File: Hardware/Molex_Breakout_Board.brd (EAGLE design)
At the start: 31.8 x 36.8 mm, 14 parts

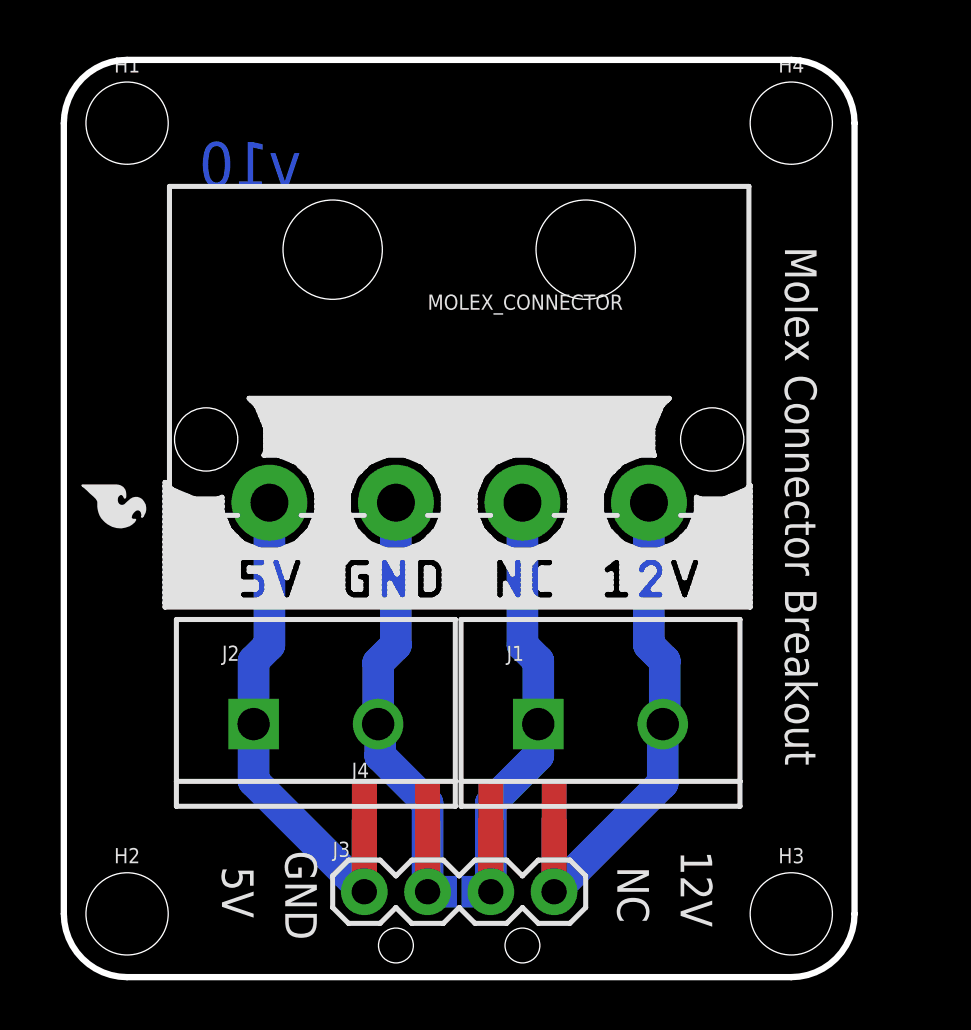
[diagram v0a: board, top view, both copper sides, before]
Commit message: Update Board File
-update text to standard buzzard
-remove negasilk and replace with dashed outline of straight molex connector
-add top thick trace on top
-adjust package so that NC is GND
-remove jumper on bottom of board
-adjust size so mounting holes are not in the way of right angle connector
-adjust measurements based on new size
-adjust text so that it is not overlapping on the mounting holes
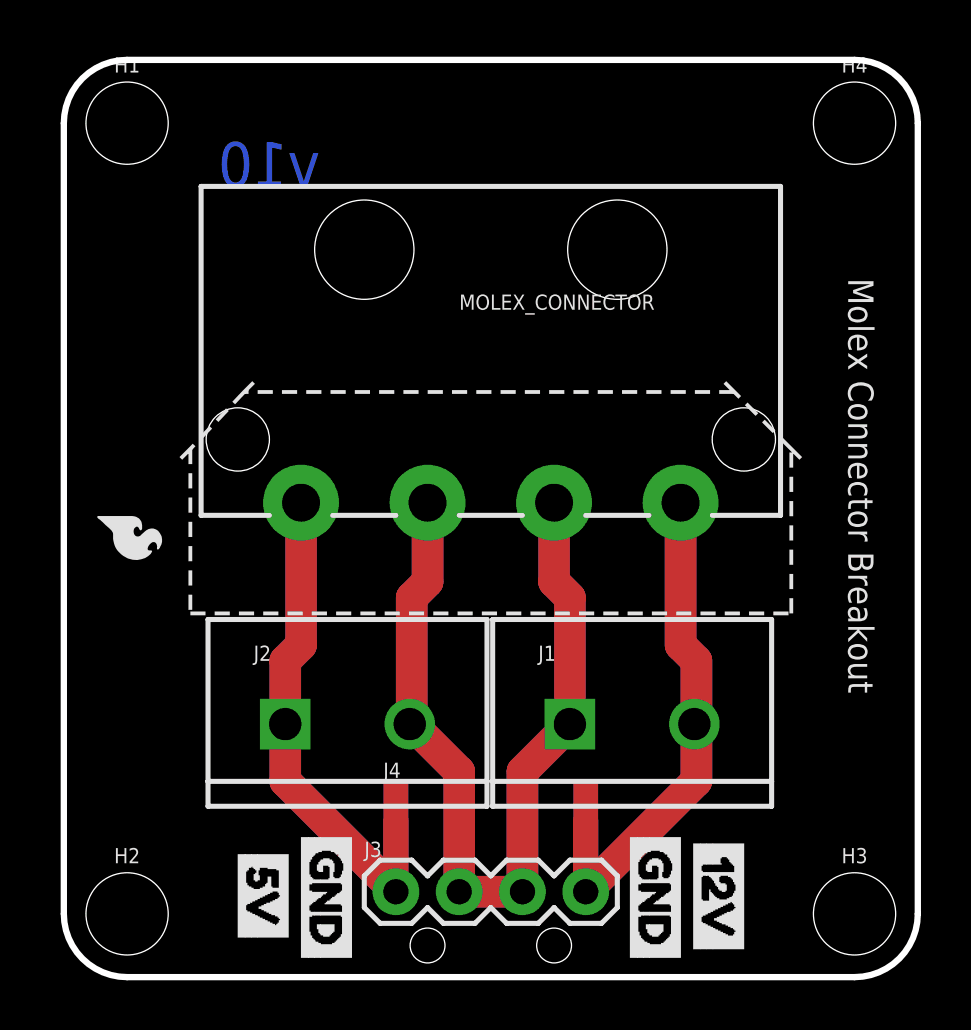
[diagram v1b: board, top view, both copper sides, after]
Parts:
- removed JP1: JUMPER-SMT_2_NO_NO-SILK, SparkFun-Jumpers:SMT-JUMPER_2_NO_NO-SILK
- moved H3 2.54 mm to (31.8, 2.54)
- moved H4 2.54 mm to (31.8, 34.3)
- moved LOGO3 1.42 mm to (1.02, 18.8)
- moved J3 1.27 mm to (13.3, 3.43)
- moved J2 1.27 mm to (8.89, 10.2)
- moved J1 1.27 mm to (20.3, 10.2)
- moved J4 1.27 mm to (17.1, 1.27)
- moved LOGO1 1.27 mm to (17.1, 27.9)
- moved LOGO2 1.27 mm to (23.5, 20.3)
- moved MOLEX_CONNECTOR 1.27 mm to (17.1, 21.6)
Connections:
- removed net NC: J1.1, J3.3, J4.3, JP1.2, MOLEX_CONNECTOR.NC
- net GND: now also J1.1, J3.3, J4.3, MOLEX_CONNECTOR.GND@1, MOLEX_CONNECTOR.GND@2; no longer JP1.1, MOLEX_CONNECTOR.GND
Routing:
- net GND: track 20.4 -> 77.8 mm
- net NC: track 20.4 -> 0.00 mm
- net 12V: track 20.6 -> 38.5 mm
- net 5V: track 20.6 -> 38.3 mm
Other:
- board size 31.8 x 36.8 mm -> 34.3 x 36.8 mm
- board text removed: "12V"
- board text removed: "5V"
- board text removed: "GND"
- board text removed: "NC"

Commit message: Update Board
-use buzzard text for board's name
-adjust ground pour "width" to 0.01" to fit SparkFun DRC standards
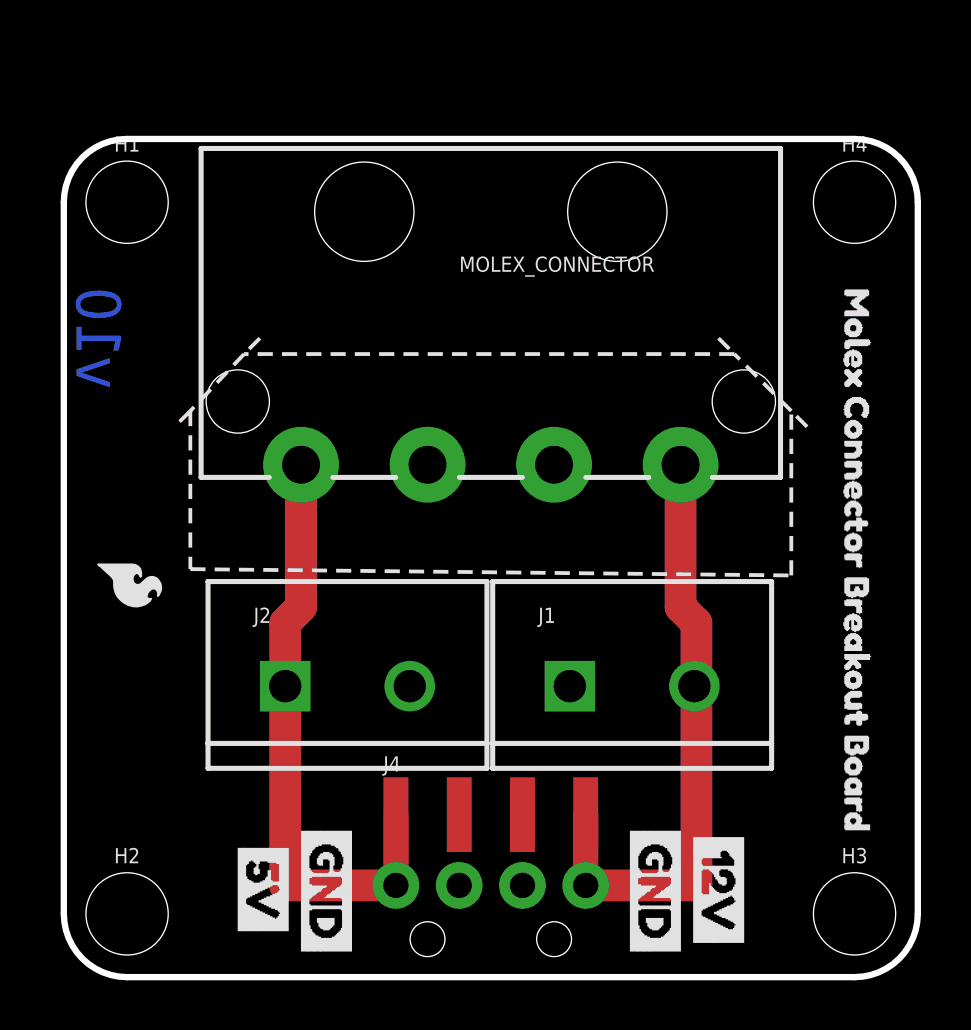
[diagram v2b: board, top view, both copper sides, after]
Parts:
- added U$1, U$5: (no value), 12V Buzzard:12V0
- added U$2, U$8: (no value), 5V Buzzard:5V0
- added U$3, U$4, U$6, U$7: (no value), GND Buzzard:GND0
- added U$9: (no value), MolexConnectorBreakout2:MOLEX_CONNECTOR_BREAKOUT_BOARD0
- moved FRAME1 6.35 mm to (-17.8, -23.5)
- moved H1 3.18 mm to (2.54, 31.1)
- moved H4 3.18 mm to (31.8, 31.1)
- moved LOGO3 1.91 mm to (1.02, 16.9)
- moved LOGO2 1.52 mm to (23.5, 21.8)
- moved MOLEX_CONNECTOR 1.52 mm to (17.1, 23.1)
- moved J1 1.52 mm to (20.3, 11.7)
- moved J2 1.52 mm to (8.89, 11.7)
- moved LOGO1 1.52 mm to (17.1, 29.5)
- moved J3 0.25 mm to (13.3, 3.68), flipped to the bottom, turned to 180 degrees
- moved J4 0.25 mm to (17.1, 1.52)
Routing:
- net GND: track 77.8 -> 0.00 mm
- net 5V: track 38.3 -> 46.0 mm
- net 12V: track 38.5 -> 46.2 mm
- added copper zone on layer 1, net GND
- added copper zone on layer 16, net GND
- removed copper zone on layer 16, net N$1
- removed copper zone on layer 1, net N$2
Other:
- board size 34.3 x 36.8 mm -> 34.3 x 33.7 mm
- board text removed: "Molex Connector Breakout"
